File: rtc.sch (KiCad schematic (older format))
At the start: 6 parts, among them U7 MCP7940N-xP, Y1 32,768 Hz

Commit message: Replace PartNum with MPN so Kicost can see it.
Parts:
- BT1: PartNo 103 -> (none); mpn (none) -> 103
- C21, C22: PartNo FG18C0G1H060DNT06 -> (none); mpn (none) -> FG18C0G1H060DNT06
- C23: PartNo K104K15X7RF5TL2 -> (none); mpn (none) -> K104K15X7RF5TL2
- U7: PartNo MCP7940N-I/P -> (none); mpn (none) -> MCP7940N-I/P
- Y1: PartNo CFS-20632768DZBB -> (none); mpn (none) -> CFS-20632768DZBB
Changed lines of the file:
@@
 F 3 "http://ww1.microchip.com/downloads/en/DeviceDoc/20005010F.pdf" H 4950 3350 50  0001 C CNN
 F 4 "Microchip" H 4950 3350 50  0001 C CNN "Manufacturer"
-F 5 "MCP7940N-I/P" H 4950 3350 50  0001 C CNN "PartNo"
+F 5 "MCP7940N-I/P" H 4950 3350 50  0001 C CNN "mpn"
 	1    4950 3350
 	1    0    0    -1
@@
 F 3 "~" V 6300 3460 50  0001 C CNN
 F 4 "Keystone" H 6300 3400 50  0001 C CNN "Manufacturer"
-F 5 "103" H 6300 3400 50  0001 C CNN "PartNo"
+F 5 "103" H 6300 3400 50  0001 C CNN "mpn"
 	1    6300 3400
 	1    0    0    -1
@@
 F 3 "~" H 7050 3350 50  0001 C CNN
 F 4 "Vishay" H 0   0   50  0001 C CNN "Manufacturer"
-F 5 "K104K15X7RF5TL2" H 0   0   50  0001 C CNN "PartNo"
+F 5 "K104K15X7RF5TL2" H 0   0   50  0001 C CNN "mpn"
 	1    7050 3350
 	1    0    0    -1
@@
 F 3 "http://cfd.citizen.co.jp/english/prod-tech/product/pdf/datasheet_TF/CFS-206_CFS-145_E.pdf" H 5550 3350 50  0001 C CNN
 F 4 "Citizen" H 5550 3350 50  0001 C CNN "Manufacturer"
-F 5 "CFS-20632768DZBB " H 5550 3350 50  0001 C CNN "PartNo"
+F 5 "CFS-20632768DZBB " H 5550 3350 50  0001 C CNN "mpn"
 	1    5550 3350
 	0    1    1    0
@@
 F 3 "~" H 5550 2950 50  0001 C CNN
 F 4 "TDK" H 0   0   50  0001 C CNN "Manufacturer"
-F 5 "FG18C0G1H060DNT06" H 0   0   50  0001 C CNN "PartNo"
+F 5 "FG18C0G1H060DNT06" H 0   0   50  0001 C CNN "mpn"
 	1    5550 2950
 	1    0    0    -1
@@
 F 3 "~" H 5550 3750 50  0001 C CNN
 F 4 "TDK" H 0   0   50  0001 C CNN "Manufacturer"
-F 5 "FG18C0G1H060DNT06" H 0   0   50  0001 C CNN "PartNo"
+F 5 "FG18C0G1H060DNT06" H 0   0   50  0001 C CNN "mpn"
 	1    5550 3750
 	1    0    0    -1

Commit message: Tweaks to the BOM.
Marking parts as DNP=1 should stop them appearing in the BOM.
Also set multi-parts for ICs in sockets.
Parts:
- BT1: DNP (none) -> 0; Manufacturer Keystone -> Keystone;Panasonic; mpn 103 -> 103;CR2032
- C21, C22, C23, Y1: DNP (none) -> 0
- U7: DNP (none) -> 0; Manufacturer Microchip -> Microchip;On Shore Technology; mpn MCP7940N-I/P -> MCP7940N-I/P;ED08DT
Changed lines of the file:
@@
 F 2 "Package_DIP:DIP-8_W7.62mm" H 4950 3350 50  0001 C CNN
 F 3 "http://ww1.microchip.com/downloads/en/DeviceDoc/20005010F.pdf" H 4950 3350 50  0001 C CNN
-F 4 "Microchip" H 4950 3350 50  0001 C CNN "Manufacturer"
-F 5 "MCP7940N-I/P" H 4950 3350 50  0001 C CNN "mpn"
+F 4 "Microchip;On Shore Technology" H 4950 3350 50  0001 C CNN "Manufacturer"
+F 5 "MCP7940N-I/P;ED08DT" H 4950 3350 50  0001 C CNN "mpn"
+F 6 "0" H 4950 3350 50  0001 C CNN "DNP"
 	1    4950 3350
 	1    0    0    -1
@@
 F 2 "Neotron 32:BatteryHolder_Keystone_103_1x20mm" V 6300 3460 50  0001 C CNN
 F 3 "~" V 6300 3460 50  0001 C CNN
-F 4 "Keystone" H 6300 3400 50  0001 C CNN "Manufacturer"
-F 5 "103" H 6300 3400 50  0001 C CNN "mpn"
+F 4 "Keystone;Panasonic" H 6300 3400 50  0001 C CNN "Manufacturer"
+F 5 "103;CR2032" H 6300 3400 50  0001 C CNN "mpn"
+F 6 "0" H 6300 3400 50  0001 C CNN "DNP"
 	1    6300 3400
 	1    0    0    -1
@@
 F 4 "Vishay" H 0   0   50  0001 C CNN "Manufacturer"
 F 5 "K104K15X7RF5TL2" H 0   0   50  0001 C CNN "mpn"
+F 6 "0" H 7050 3350 50  0001 C CNN "DNP"
 	1    7050 3350
 	1    0    0    -1
@@
 F 4 "Citizen" H 5550 3350 50  0001 C CNN "Manufacturer"
 F 5 "CFS-20632768DZBB " H 5550 3350 50  0001 C CNN "mpn"
+F 6 "0" H 5550 3350 50  0001 C CNN "DNP"
 	1    5550 3350
 	0    1    1    0
@@
 F 4 "TDK" H 0   0   50  0001 C CNN "Manufacturer"
 F 5 "FG18C0G1H060DNT06" H 0   0   50  0001 C CNN "mpn"
+F 6 "0" H 5550 2950 50  0001 C CNN "DNP"
 	1    5550 2950
 	1    0    0    -1
@@
 F 4 "TDK" H 0   0   50  0001 C CNN "Manufacturer"
 F 5 "FG18C0G1H060DNT06" H 0   0   50  0001 C CNN "mpn"
+F 6 "0" H 5550 3750 50  0001 C CNN "DNP"
 	1    5550 3750
 	1    0    0    -1

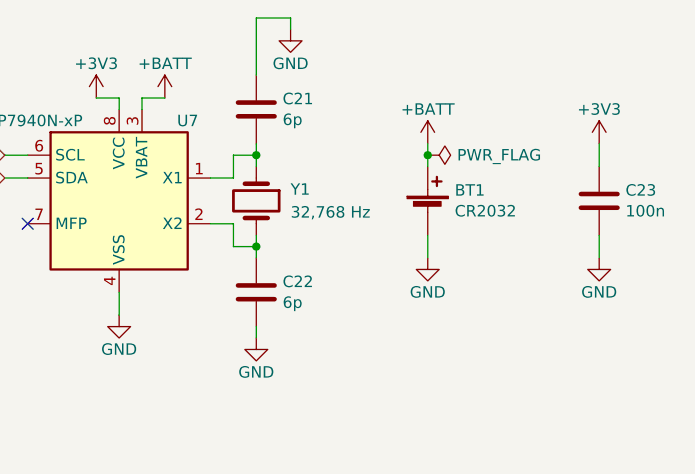
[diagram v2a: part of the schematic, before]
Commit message: Cleaned up Atmega reset. Set hold size to 3.5mm, so M3 screws go through nicely Reset numbering to page x 100 Renamed Launchpad to EK-TM4C123GXL Renamed top-level signals to KBMS page as KBMS_TO/FROM_MCU
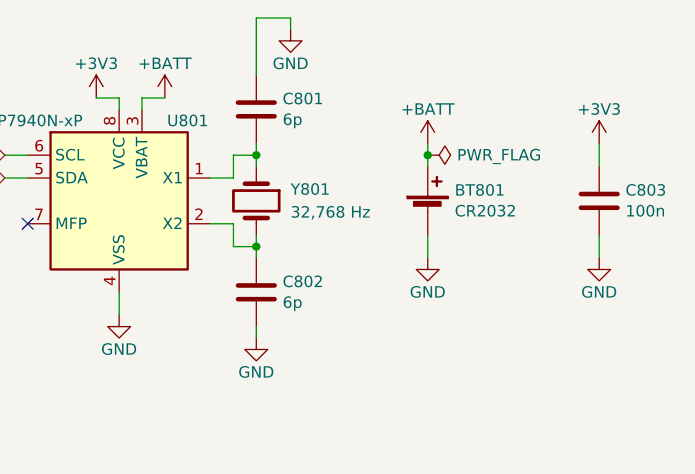
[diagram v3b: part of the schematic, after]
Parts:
- renumbered BT1 to BT801, C21 to C801, C22 to C802, C23 to C803, U7 to U801, Y1 to Y801
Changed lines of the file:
@@
 MCU_I2C_SCL
 $Comp
-L Timer:MCP7940N-xP U7
+L Timer:MCP7940N-xP U801
 U 1 1 5E0F47D7
 P 4950 3350
-F 0 "U7" H 5250 3700 50  0000 C CNN
+F 0 "U801" H 5250 3700 50  0000 C CNN
 F 1 "MCP7940N-xP" H 4550 3700 50  0000 C CNN
 F 2 "Package_DIP:DIP-8_W7.62mm" H 4950 3350 50  0001 C CNN
@@
 $EndComp
 $Comp
-L Device:Battery_Cell BT1
+L Device:Battery_Cell BT801
 U 1 1 5E0F507E
 P 6300 3400
-F 0 "BT1" H 6418 3496 50  0000 L CNN
+F 0 "BT801" H 6418 3496 50  0000 L CNN
 F 1 "CR2032" H 6418 3405 50  0000 L CNN
 F 2 "Neotron 32:BatteryHolder_Keystone_103_1x20mm" V 6300 3460 50  0001 C CNN
@@
 P 7050 3350
 AR Path="/5DF1D0B0/5E0203CB" Ref="C?"  Part="1"
-AR Path="/5DF66898/5E0203CB" Ref="C23"  Part="1"
-F 0 "C23" H 7165 3396 50  0000 L CNN
+AR Path="/5DF66898/5E0203CB" Ref="C803"  Part="1"
+F 0 "C803" H 7165 3396 50  0000 L CNN
 F 1 "100n" H 7165 3305 50  0000 L CNN
 F 2 "Capacitor_THT:C_Disc_D3.0mm_W2.0mm_P2.50mm" H 7088 3200 50  0001 C CNN
@@
 $EndComp
 $Comp
-L Device:Crystal Y1
+L Device:Crystal Y801
 U 1 1 5E028A76
 P 5550 3350
-F 0 "Y1" V 5500 3500 50  0000 L CNN
+F 0 "Y801" V 5500 3500 50  0000 L CNN
 F 1 "32,768 Hz" V 5600 3500 50  0000 L CNN
 F 2 "Crystal:Crystal_C26-LF_D2.1mm_L6.5mm_Horizontal" H 5550 3350 50  0001 C CNN
@@
 	6300 3500 6300 3600
 $Comp
-L Device:C C21
+L Device:C C801
 U 1 1 5E02C5CE
 P 5550 2950
-F 0 "C21" H 5665 2996 50  0000 L CNN
+F 0 "C801" H 5665 2996 50  0000 L CNN
 F 1 "6p" H 5665 2905 50  0000 L CNN
 F 2 "Capacitor_THT:C_Disc_D3.0mm_W2.0mm_P2.50mm" H 5588 2800 50  0001 C CNN
@@
 $EndComp
 $Comp
-L Device:C C22
+L Device:C C802
 U 1 1 5E02CC31
 P 5550 3750
-F 0 "C22" H 5665 3796 50  0000 L CNN
+F 0 "C802" H 5665 3796 50  0000 L CNN
 F 1 "6p" H 5665 3705 50  0000 L CNN
 F 2 "Capacitor_THT:C_Disc_D3.0mm_W2.0mm_P2.50mm" H 5588 3600 50  0001 C CNN
